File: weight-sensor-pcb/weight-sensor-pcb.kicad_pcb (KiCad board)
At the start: 2 copper layers, 14 parts, among them IC1 SN65HVD230DR, J1 TC2030, J2 54602-908LF, J4 Conn_01x05_Pin, U4 STM32F042F4P6

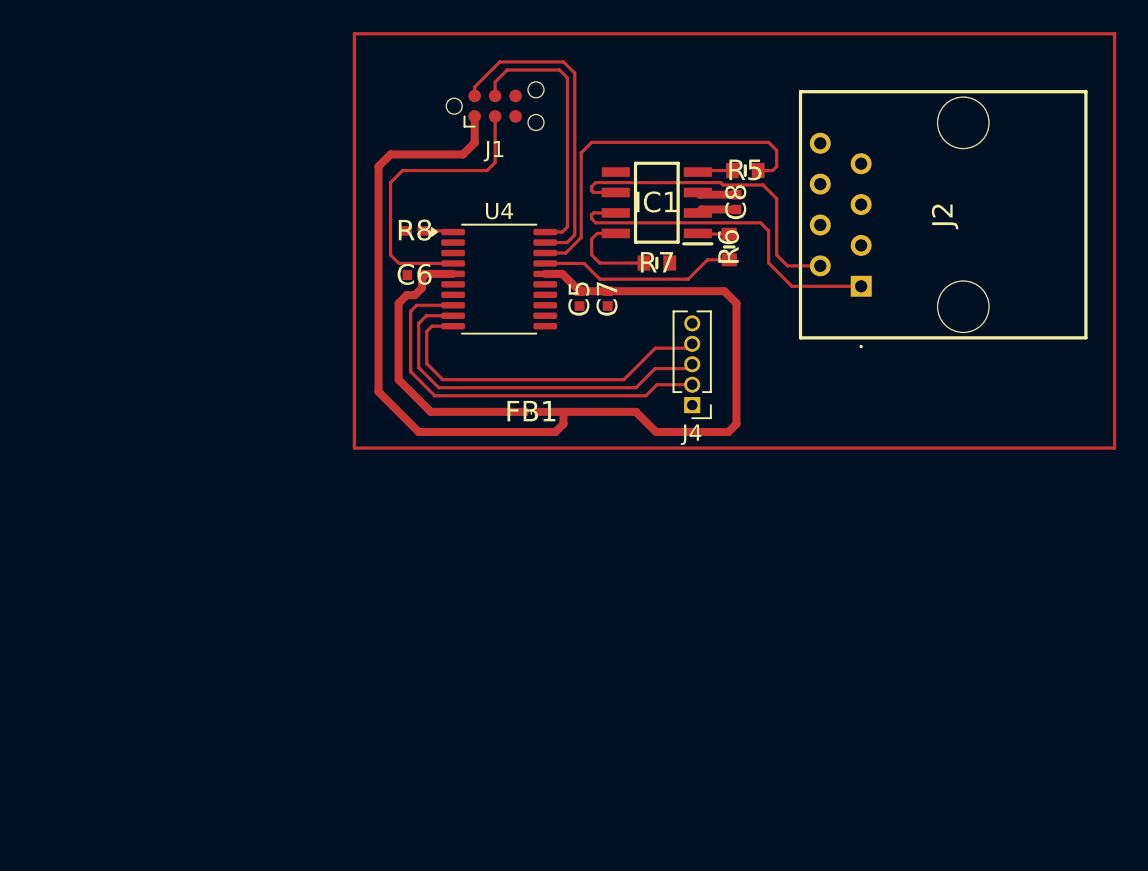
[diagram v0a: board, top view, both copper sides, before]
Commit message: update CAN transceiver schematic/layout, use env vars for library paths
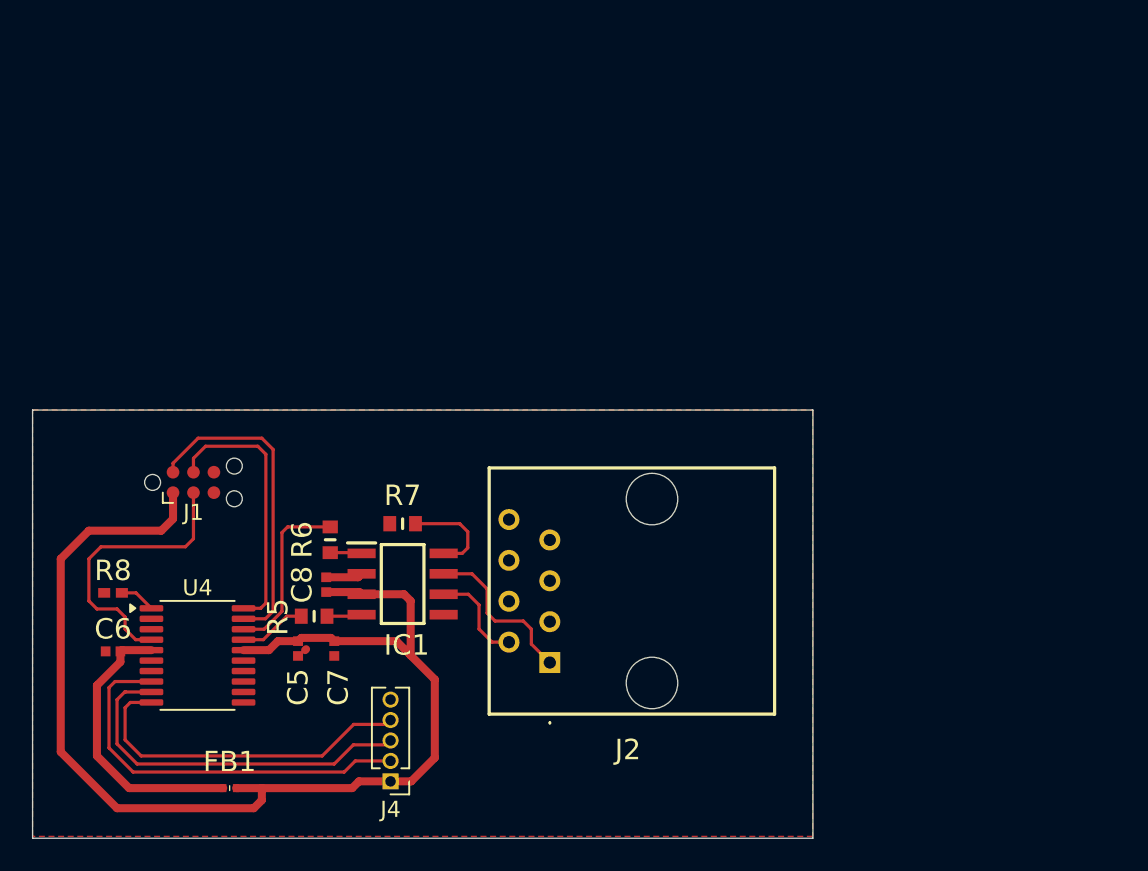
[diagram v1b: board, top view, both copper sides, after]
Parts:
- moved R5 38.5 mm to (141.0, 99.5), turned to 0 degrees
- moved C8 34.9 mm to (141.8, 97.5), turned to 90 degrees
- moved R6 30.8 mm to (142.0, 94.7), turned to -90 degrees
- moved J2 30.4 mm to (155.7, 102.3)
- moved C6 30.0 mm to (128.5, 101.6)
- moved FB1 30.0 mm to (135.8, 110.1)
- moved J1 30.0 mm to (133.5, 91.1)
- moved J4 30.0 mm to (145.8, 109.7)
- moved U4 30.0 mm to (133.8, 101.9)
- moved R8 29.3 mm to (128.5, 98.0)
- moved IC1 28.5 mm to (146.5, 97.5), turned to 0 degrees
- moved C5 27.9 mm to (140.0, 101.5)
- moved C7 27.6 mm to (142.2, 101.5)
- moved R7 22.6 mm to (146.5, 93.7), turned to 0 degrees
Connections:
- U4 pad 17: /CAN Interface/CAN_TX -> /CAN Interface/CAN_RX
- U4 pad 18: /CAN Interface/CAN_RX -> /CAN Interface/CAN_TX
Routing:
- net /CAN Interface/CAN_RX: track 24.7 -> 6.38 mm
- net /CAN Interface/CAN_L: track 20.3 -> 6.17 mm
- net /CAN Interface/CAN_H: track 21.5 -> 10.3 mm
- net +3.3V: track 71.4 -> 76.7 mm
- net /CAN Interface/CAN_TX: track 12.3 -> 10.9 mm
- net /STM32 Microcontroller/NRST: track 18.5 -> 17.8 mm
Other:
- board outline added: 48.5 x 26.6 mm
